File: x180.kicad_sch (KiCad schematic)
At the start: 73 parts, among them J1 U180 Header, J2 Conn_01x06_Pin, U1 ATF1502AS-7A, U2 ADG734, U3 ADG734, U4 ADG734, U5 ADG734

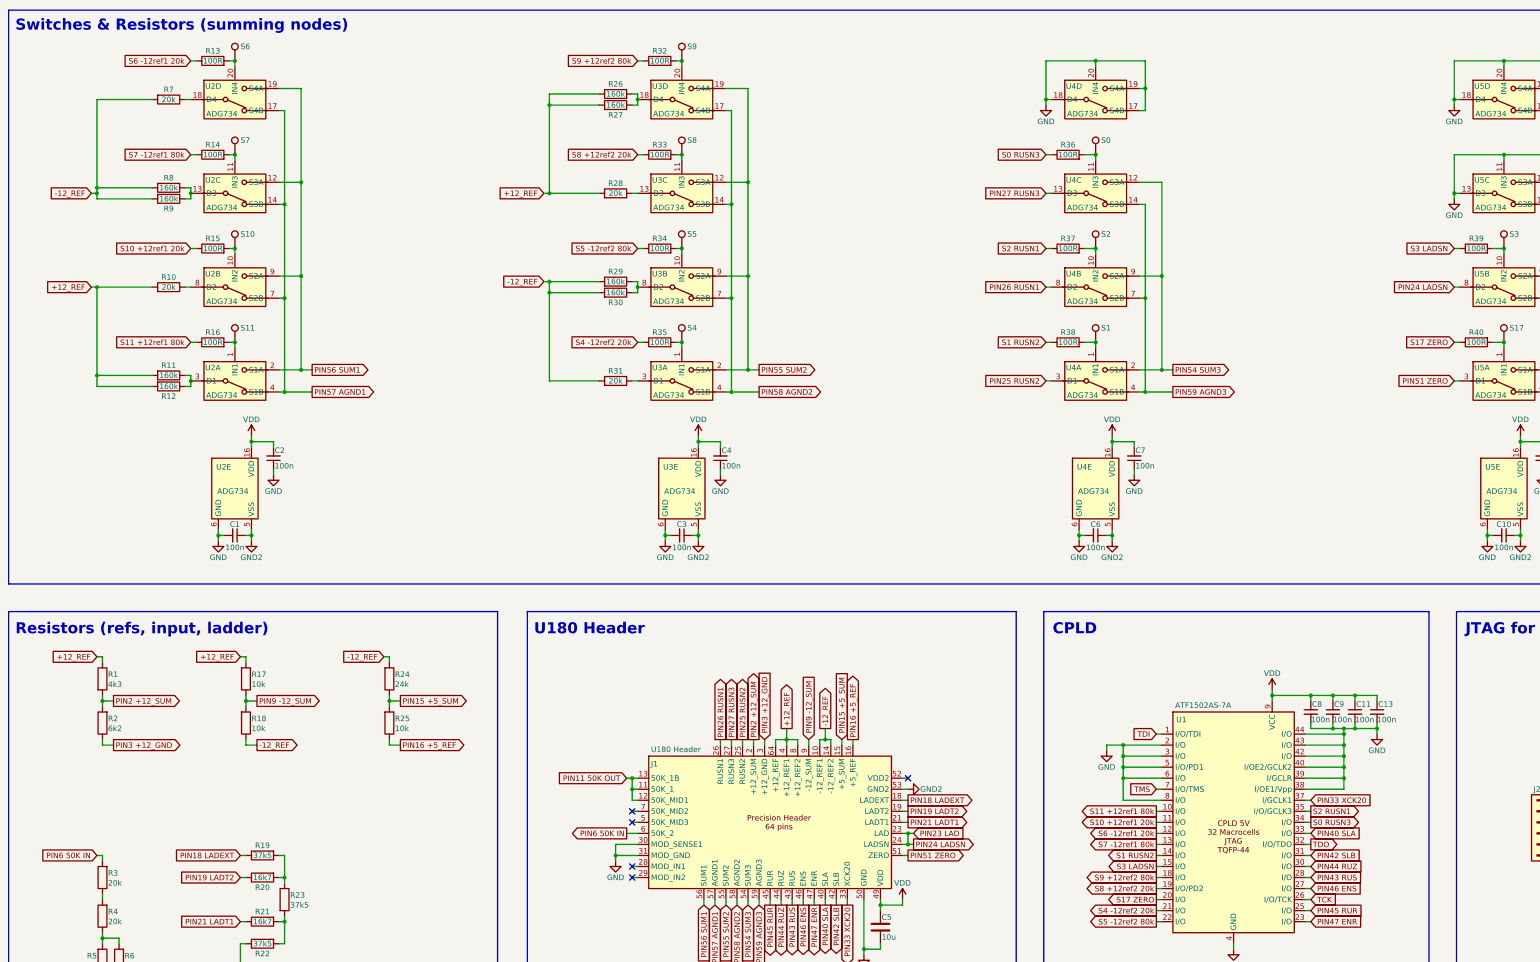
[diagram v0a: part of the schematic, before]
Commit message: Update of PCB
Update with pulldowns for the control lines and the option to use gate modulation. Also added CPLD code with pinkeep disabled. (Required for linearity, one needs to connect the JTAG lines to GND after programing.)
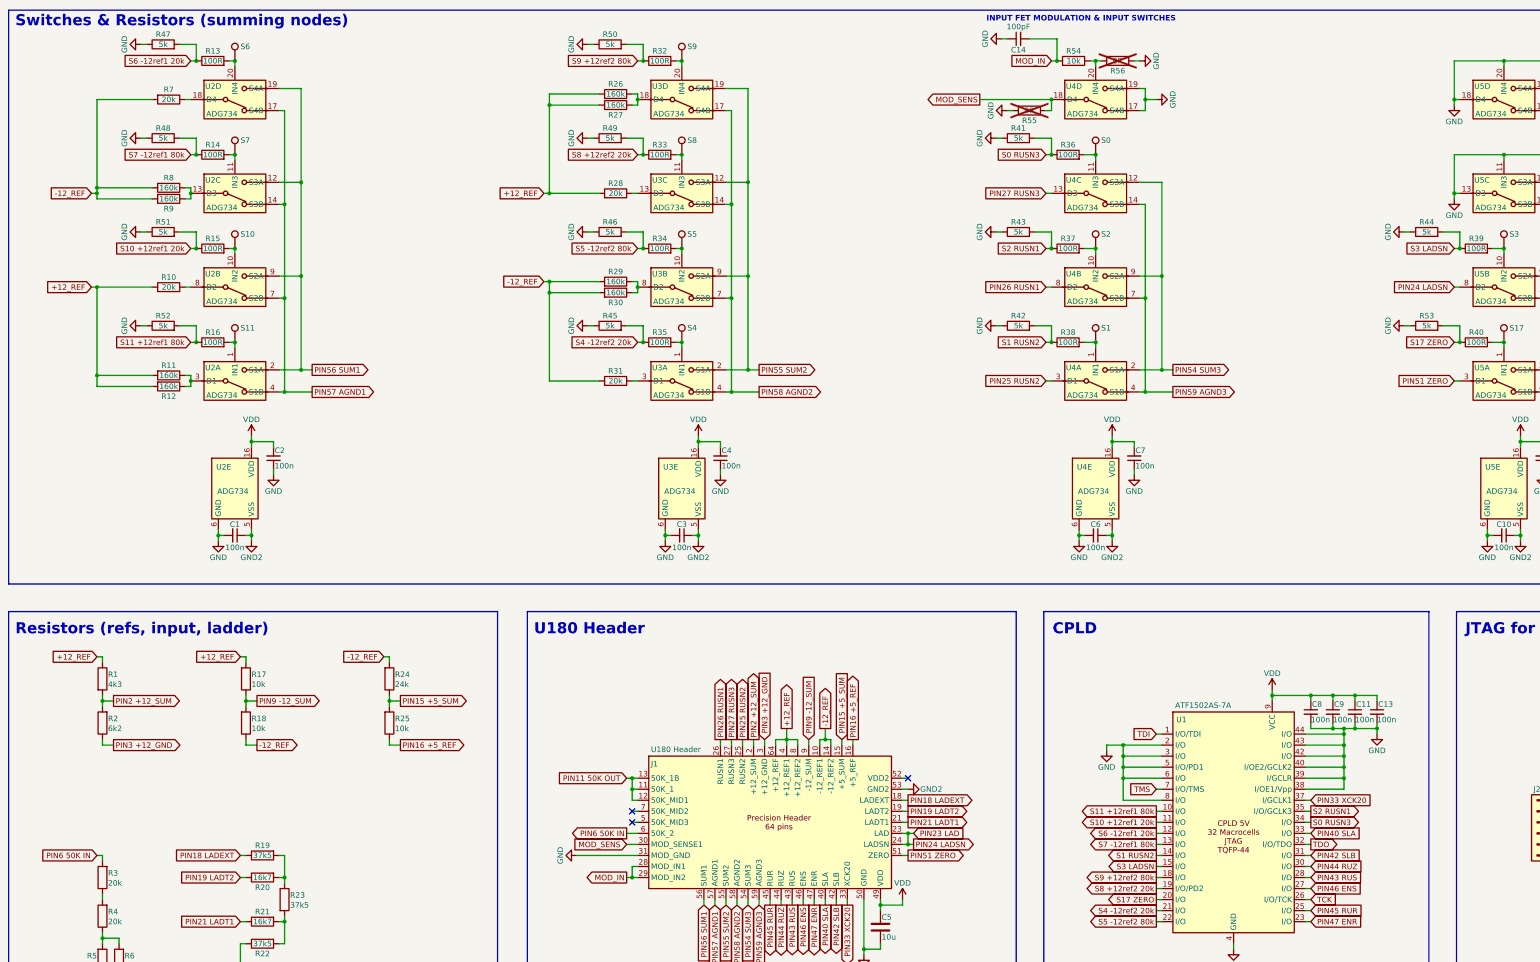
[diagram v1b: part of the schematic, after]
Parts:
- added C14: 100pF, Capacitor_SMD:C_0603_1608Metric, symbol Device:C_Small
- added R41, R42, R43, R44, R45, R46, R47, R48, R49, R50, R51, R52, R53: 5k, Resistor_SMD:R_0603_1608Metric, symbol Device:R
- added R54: 10k, Resistor_SMD:R_0603_1608Metric, symbol Device:R
- added R55, R56: 0R, Resistor_SMD:R_0603_1608Metric, symbol Device:R
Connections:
- net GND: now also C14.1, R41.1, R42.1, R43.1, R44.1, R45.1, R46.1, R47.1, R48.1, R49.1, R50.1, R51.1, R52.1, R53.1, R55.2, R56.1; no longer J1.30 (MOD_SENSE1), U4.18 (D4), U4.20 (IN4)
- net S0 RUSN3: now also R41.2
- net S1 RUSN2: now also R42.2
- net S10 +12ref1 20k: now also R51.2
- net S11 +12ref1 80k: now also R52.2
- net S17 ZERO: now also R53.2
- net S2 RUSN1: now also R43.2
- net S3 LADSN: now also R44.2
- net S4 -12ref2 20k: now also R45.2
- net S5 -12ref2 80k: now also R46.2
- net S6 -12ref1 20k: now also R47.2
- net S7 -12ref1 80k: now also R48.2
- net S8 +12ref2 20k: now also R49.2
- net S9 +12ref2 80k: now also R50.2
- net MOD_IN: now reaches J1.28 (MOD_IN1)
- net MOD_IN: now also J1.29 (MOD_IN2), C14.2, R54.2
- new net: R54.1, R56.2, U4.20 (IN4)
- new net MOD_SENS: J1.30 (MOD_SENSE1), R55.1, U4.18 (D4)
- no-connect marks 5 -> 3
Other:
- note added: "INPUT FET MODULATION & INPUT SWITCHES"

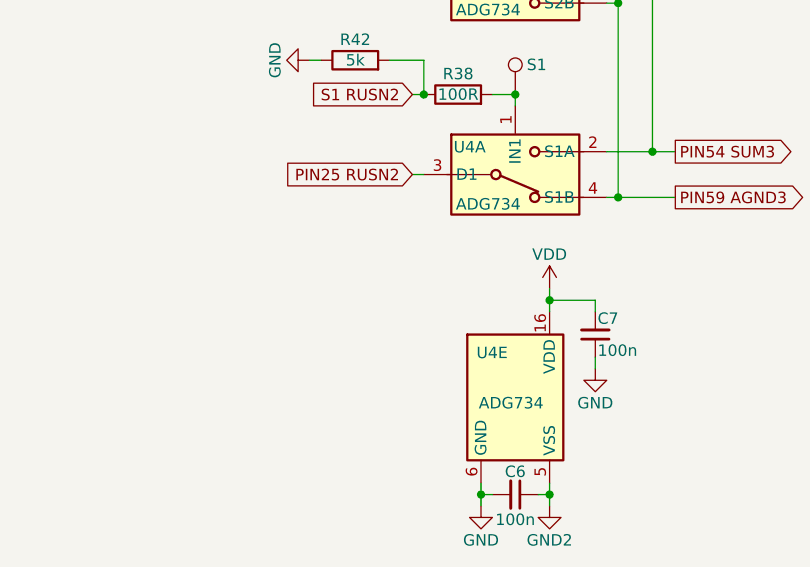
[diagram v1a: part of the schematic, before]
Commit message: Fixed the gate voltage modulation
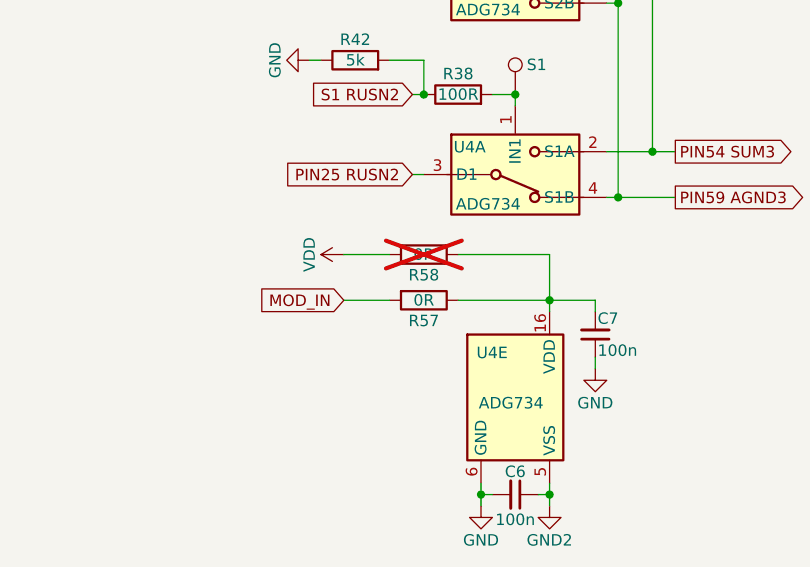
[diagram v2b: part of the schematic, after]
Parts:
- added R57, R58: 0R, Resistor_SMD:R_0402_1005Metric, symbol Device:R
- R55, R56: footprint Resistor_SMD:R_0603_1608Metric -> Resistor_SMD:R_0402_1005Metric
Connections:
- net MOD_IN: now also R57.2
- net VCC: now also R58.2; no longer C7.2, U4.16 (VDD)
- new net: C7.2, R57.1, R58.1, U4.16 (VDD)
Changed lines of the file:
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@@
 	)
 	(junction
+		(at 273.05 116.84)
+		(diameter 0)
+		(color 0 0 0 0)
+	)
+	(junction
 		(at 269.24 72.39)
 		(diameter 0)
@@
 	)
 	(junction
-		(at 273.05 116.84)
-		(diameter 0)
-		(color 0 0 0 0)
-	)
-	(junction
 		(at 374.65 57.15)
 		(diameter 0)
@@
 	(wire
 		(pts
+			(xy 250.19 111.76) (xy 255.27 111.76)
+		)
+		(stroke
+			(width 0)
+			(type default)
+		)
+	)
+	(wire
+		(pts
 			(xy 39.37 101.6) (xy 52.07 101.6)
 		)
@@
 	(wire
 		(pts
+			(xy 273.05 111.76) (xy 273.05 116.84)
+		)
+		(stroke
+			(width 0)
+			(type default)
+		)
+	)
+	(wire
+		(pts
 			(xy 363.22 29.21) (xy 363.22 30.48)
 		)
@@
 	(wire
 		(pts
+			(xy 250.19 116.84) (xy 255.27 116.84)
+		)
+		(stroke
+			(width 0)
+			(type default)
+		)
+	)
+	(wire
+		(pts
 			(xy 143.51 39.37) (xy 143.51 59.69)
 		)
@@
 	(wire
 		(pts
-			(xy 273.05 115.57) (xy 273.05 116.84)
-		)
-		(stroke
-			(width 0)
-			(type default)
-		)
-	)
-	(wire
-		(pts
 			(xy 143.51 82.55) (xy 143.51 102.87)
 		)
@@
 	(wire
 		(pts
+			(xy 262.89 116.84) (xy 273.05 116.84)
+		)
+		(stroke
+			(width 0)
+			(type default)
+		)
+	)
+	(wire
+		(pts
 			(xy 300.99 232.41) (xy 300.99 233.68)
 		)
@@
 	(wire
 		(pts
+			(xy 262.89 111.76) (xy 273.05 111.76)
+		)
+		(stroke
+			(width 0)
+			(type default)
+		)
+	)
+	(wire
+		(pts
 			(xy 82.55 217.17) (xy 82.55 218.44)
 		)
@@
 		)
 	)
+	(global_label "MOD_IN"
+		(shape input)
+		(at 250.19 116.84 180)
+		(fields_autoplaced yes)
+		(effects
+			(font
+				(size 1.27 1.27)
+			)
+			(justify right)
+		)
+		(property "Intersheetrefs" "${INTERSHEET_REFS}"
+			(at 240.25 116.84 0)
+			(effects
+				(font
+					(size 1.27 1.27)
+				)
+				(justify right)
+				(hide yes)
+			)
+		)
+	)
 	(global_label "S11 +12ref1 80k"
 		(shape output)
@@
 			)
 		)
-		(property "Footprint" "Resistor_SMD:R_0603_1608Metric"
+		(property "Footprint" "Resistor_SMD:R_0402_1005Metric"
 			(at 254 38.862 90)
 			(effects
@@
 	(symbol
 		(lib_id "Device:R")
+		(at 259.08 111.76 270)
+		(unit 1)
+		(exclude_from_sim no)
+		(in_bom yes)
+		(on_board yes)
+		(dnp yes)
+		(property "Reference" "R58"
+			(at 259.08 114.046 90)
+			(effects
+				(font
+					(size 1.27 1.27)
+				)
+			)
+		)
+		(property "Value" "0R"
+			(at 259.08 111.76 90)
+			(effects
+				(font
+					(size 1.27 1.27)
+				)
+			)
+		)
+		(property "Footprint" "Resistor_SMD:R_0402_1005Metric"
+			(at 259.08 109.982 90)
+			(effects
+				(font
+					(size 1.27 1.27)
+				)
+				(hide yes)
+			)
+		)
+		(property "Datasheet" ""
+			(at 259.08 111.76 0)
+			(effects
+				(font
+					(size 1.27 1.27)
+				)
+				(hide yes)
+			)
+		)
+		(property "Description" "Resistor"
+			(at 259.08 111.76 0)
+			(effects
+				(font
+					(size 1.27 1.27)
+				)
+				(hide yes)
+			)
+		)
+		(property "Type" ""
+			(at 259.08 111.76 90)
+			(effects
+				(font
+					(size 1.27 1.27)
+				)
+				(hide yes)
+			)
+		)
+		(pin "2"
+		)
+		(pin "1"
+		)
+		(instances
+			(project "x180"
+				(path "/18c24007-ed0a-48d4-81b0-f69de71b0743"
+					(reference "R58")
+					(unit 1)
+				)
+			)
+		)
+	)
+	(symbol
+		(lib_id "Device:R")
 		(at 66.04 72.39 90)
 		(unit 1)
@@
 	(symbol
 		(lib_id "power:VDD")
-		(at 273.05 115.57 0)
-		(mirror y)
+		(at 250.19 111.76 90)
+		(mirror x)
 		(unit 1)
 		(exclude_from_sim no)
@@
 		(dnp no)
 		(property "Reference" "#PWR015"
-			(at 273.05 119.38 0)
+			(at 254 111.76 0)
 			(effects
 				(font
@@
 		)
 		(property "Value" "VDD"
-			(at 273.05 111.76 0)
+			(at 246.38 111.76 0)
 			(effects
 				(font
@@
 		)
 		(property "Footprint" ""
-			(at 273.05 115.57 0)
+			(at 250.19 111.76 0)
 			(effects
 				(font
@@
 		)
 		(property "Datasheet" ""
-			(at 273.05 115.57 0)
+			(at 250.19 111.76 0)
 			(effects
 				(font
@@
 		)
 		(property "Description" "Power symbol creates a global label with name \"VDD\""
-			(at 273.05 115.57 0)
+			(at 250.19 111.76 0)
 			(effects
 				(font
@@
 			)
 		)
-		(property "Footprint" "Resistor_SMD:R_0603_1608Metric"
+		(property "Footprint" "Resistor_SMD:R_0402_1005Metric"
 			(at 274.32 27.432 90)
 			(effects
@@
 					(unit 1)
 				)
+			)
+		)
+	)
+	(symbol
+		(lib_id "Device:R")
+		(at 259.08 116.84 270)
+		(unit 1)
+		(exclude_from_sim no)
+		(in_bom yes)
+		(on_board yes)
+		(dnp no)
+		(property "Reference" "R57"
+			(at 259.08 119.126 90)
+			(effects
+				(font
+					(size 1.27 1.27)
+				)
+			)
+		)
+		(property "Value" "0R"
+			(at 259.08 116.84 90)
+			(effects
+				(font
+					(size 1.27 1.27)
+				)
+			)
+		)
+		(property "Footprint" "Resistor_SMD:R_0402_1005Metric"
+			(at 259.08 115.062 90)
+			(effects
+				(font
+					(size 1.27 1.27)
+				)
+				(hide yes)
+			)
+		)
+		(property "Datasheet" ""
+			(at 259.08 116.84 0)
+			(effects
+				(font
+					(size 1.27 1.27)
+				)
+				(hide yes)
+			)
+		)
+		(property "Description" "Resistor"
+			(at 259.08 116.84 0)
+			(effects
+				(font
+					(size 1.27 1.27)
+				)
+				(hide yes)
+			)
+		)
+		(property "Type" ""
+			(at 259.08 116.84 90)
+			(effects
+				(font
+					(size 1.27 1.27)
+				)
+				(hide yes)
+			)
+		)
+		(pin "2"
+		)
+		(pin "1"
+		)
+		(instances
+			(project "x180"
+				(path "/18c24007-ed0a-48d4-81b0-f69de71b0743"
+					(reference "R57")
+					(unit 1)
+				)
